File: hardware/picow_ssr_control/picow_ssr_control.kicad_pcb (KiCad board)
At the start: 2 copper layers, 65 x 90 mm, 33 parts, among them Q1 DMG2301L, Q2 DMG2301L, U1 RaspberryPi-PicoW, U2 ULN2803A

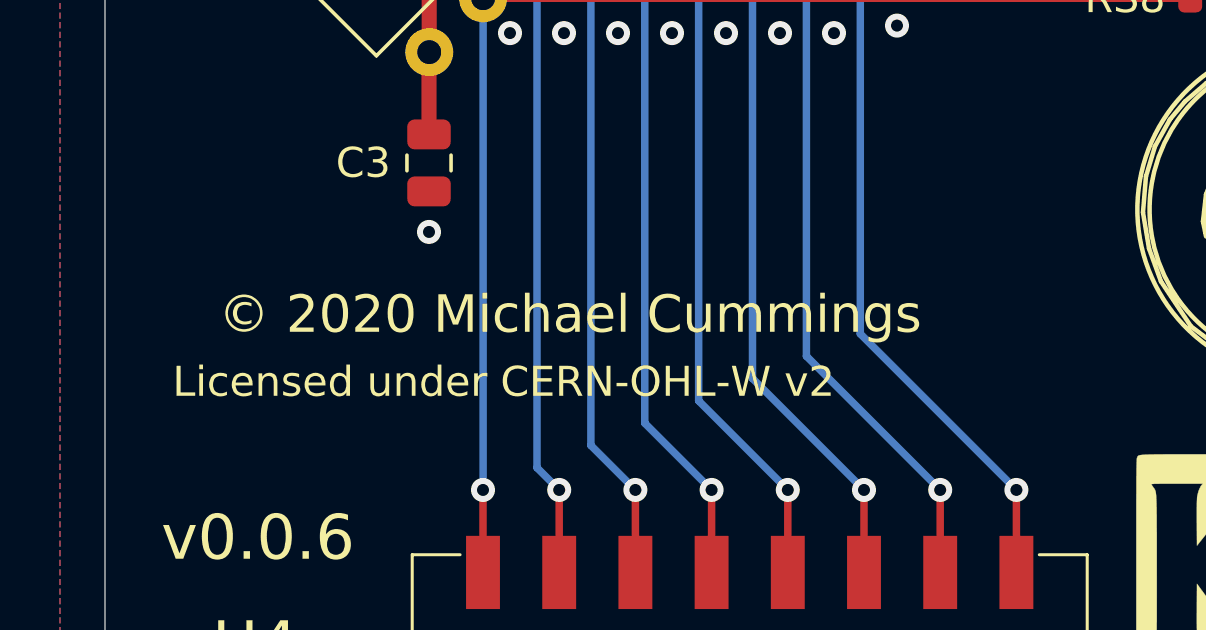
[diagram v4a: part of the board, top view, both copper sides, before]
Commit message: Fixed incorrect copyright date on PCB
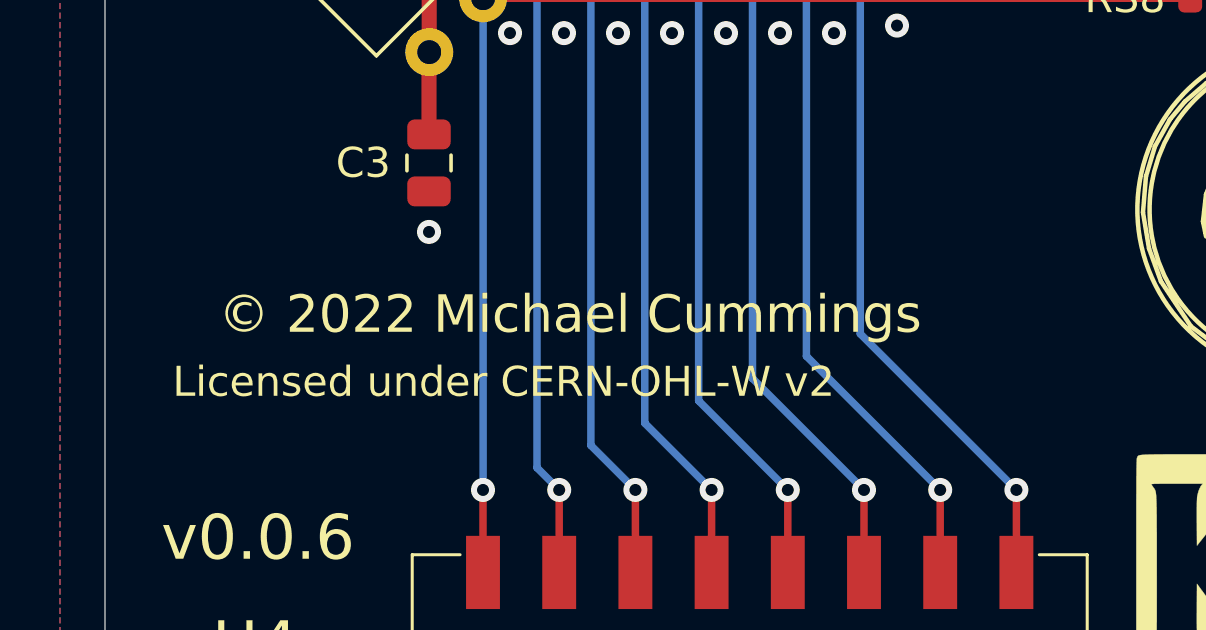
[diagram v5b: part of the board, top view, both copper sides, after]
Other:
- board text added: "© 2022 Michael Cummings"
- board text removed: "© 2020 Michael Cummings"
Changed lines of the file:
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@@
   (gr_rect (start 50 50) (end 115 140) (layer "User.9") (width 0.15) (fill none))
   (gr_circle (center 110 135) (end 111.55 135) (layer "User.9") (width 0.15) (fill none))
-  (gr_text "© 2020 Michael Cummings" (at 65.5 119.5) (layer "F.SilkS")
+  (gr_text "© 2022 Michael Cummings" (at 65.5 119.5) (layer "F.SilkS")
     (effects (font (size 1.25 1.25) (thickness 0.25)))
   )

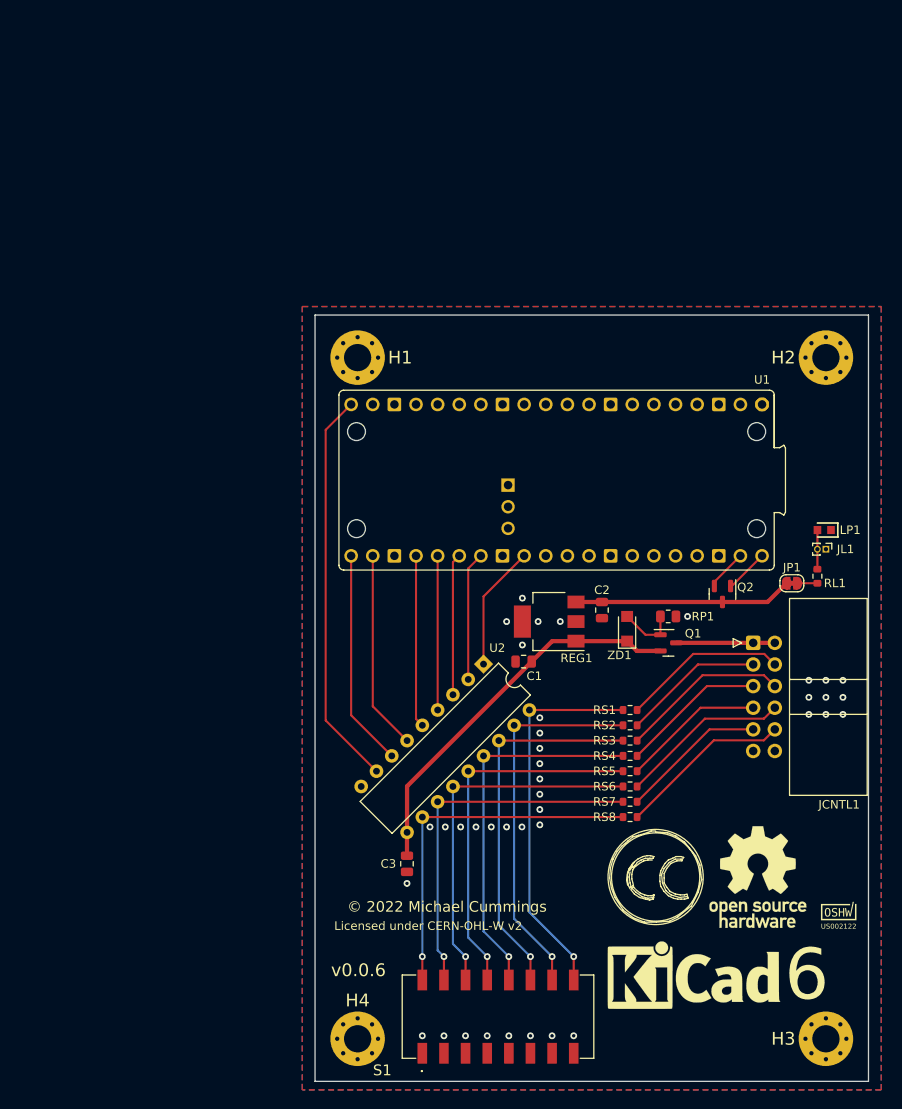
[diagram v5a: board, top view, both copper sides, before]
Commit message: WIP control connector changes v0.0.7
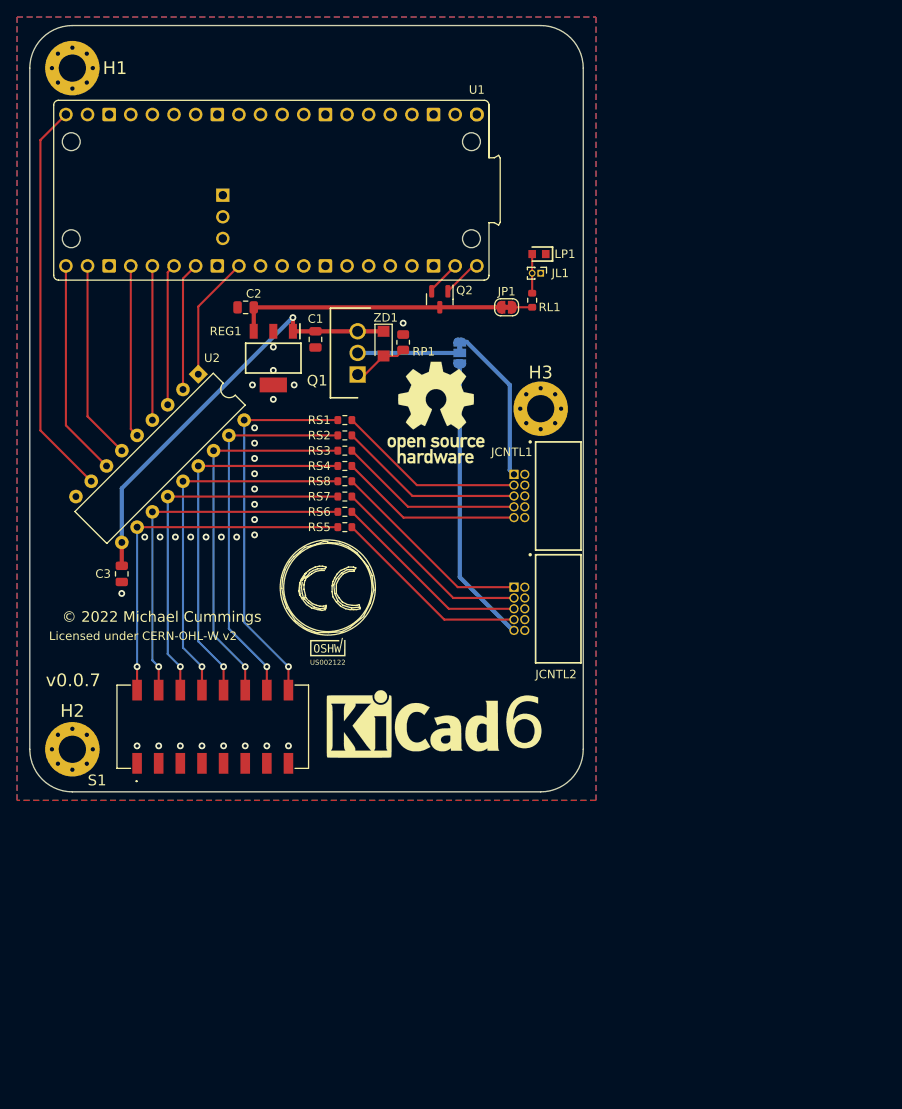
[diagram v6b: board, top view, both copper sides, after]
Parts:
- removed H4: MountingHole_Pad, MountingHole:MountingHole_3.2mm_M3_Pad_Via
- added JCNTL2: SHF-105-01-L-D-RA, dragon_mobile:SAMTEC_SHF-105-01-L-D-RA, F.Cu at (74.0, 84.5)
- added JS1: SolderJumper_3_Bridged12, Jumper:SolderJumper-3_P1.3mm_Bridged12_RoundedPad1.0x1.5mm_NumberLabels, B.Cu at (67.0, 54.5)
- JCNTL1: value Conn_02x06_Odd_Even -> SHF-105-01-L-D-RA; footprint Connector_IDC:IDC-Header_2x06_P2.54mm_Horizontal -> dragon_mobile:SAMTEC_SHF-105-01-L-D-RA
- Q1: value DMG2301L -> IRF4905PBF; footprint Package_TO_SOT_SMD:SOT-23 -> dragon_mobile:TO254P469X1042X1967-3P
- Q2: footprint Package_TO_SOT_SMD:SOT-23 -> Picow_control:DMG2301L
- REG1: footprint Package_TO_SOT_SMD:SOT-223 -> SamacSys_Parts:SOT230P700X180-4N
- RS1, RS2, RS3, RS4: value 25 -> 270
- RS5: renamed from RS8; value 25 -> 270
- RS6: renamed from RS7; value 25 -> 270
- RS7: renamed from RS6; value 25 -> 270
- RS8: renamed from RS5; value 25 -> 270
- moved H2 99.7 mm to (21.5, 101.0)
- moved H3 81.2 mm to (76.5, 61.0)
- moved OSHW_Mono_0.1_Scale 67.5 mm to (51.5, 89.0)
- moved #LOGO1 66.4 mm to (64.2, 61.5)
- moved C2 54.9 mm to (41.9, 49.1), turned to 180 degrees
- moved #LOGO2 51.4 mm to (51.5, 82.0)
- moved Q1 48.2 mm to (55.0, 57.0), turned to 90 degrees
- moved Q2 48.0 mm to (64.7, 48.1)
- moved RS1 47.8 mm to (53.5, 62.3), turned to 0 degrees
- moved S1 47.8 mm to (38.0, 98.3)
- moved U2 47.8 mm to (36.3, 57.0)
- moved C3 47.8 mm to (27.3, 80.4)
- moved QRCode1 47.8 mm to (55.2, 77.0)
- moved RS2 47.8 mm to (53.5, 64.1)
- moved RS3 47.8 mm to (53.5, 65.9), turned to 0 degrees
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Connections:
- JCNTL1 pad 1: +BATT -> Net-(JCNTL1-Pad1)
- JCNTL1 pad 10: Net-(JCNTL1-Pad10) -> GNDPWR
- JCNTL1 pad 2: +BATT -> GNDPWR
- JCNTL1 pad 4: Net-(JCNTL1-Pad4) -> GNDPWR
- JCNTL1 pad 6: Net-(JCNTL1-Pad6) -> GNDPWR
- JCNTL1 pad 8: Net-(JCNTL1-Pad8) -> GNDPWR
- Q1 pad 2: +VDC -> +BATT
- Q1 pad 3: +BATT -> +VDC
- RS1 pad 1: Net-(JCNTL1-Pad4) -> /a1
- RS1 pad 2: /a1 -> Net-(JCNTL1-Pad3)
- RS2 pad 2: Net-(JCNTL1-Pad3) -> Net-(JCNTL1-Pad5)
- RS3 pad 1: Net-(JCNTL1-Pad6) -> /a3
- RS3 pad 2: /a3 -> Net-(JCNTL1-Pad7)
- RS4 pad 1: /a4 -> Net-(JCNTL1-Pad9)
- RS4 pad 2: Net-(JCNTL1-Pad5) -> /a4
- RS5 pad 1: Net-(JCNTL1-Pad10) -> /a5
- RS5 pad 2: /a8 -> Net-(JCNTL2-Pad7)
- RS6 pad 1: /a7 -> /a6
- RS6 pad 2: Net-(JCNTL1-Pad9) -> Net-(JCNTL2-Pad5)
- RS7 pad 1: Net-(JCNTL1-Pad8) -> /a7
- RS7 pad 2: /a6 -> Net-(JCNTL2-Pad3)
- RS8 pad 1: /a5 -> /a8
- RS8 pad 2: Net-(JCNTL1-Pad7) -> Net-(JCNTL2-Pad1)
- S1 pad 13: /a5 -> /a8
- S1 pad 14: /a6 -> /a7
- S1 pad 15: /a7 -> /a6
- S1 pad 16: /a8 -> /a5
- U2 pad 11: /a8 -> /a5
- U2 pad 12: /a7 -> /a6
- U2 pad 13: /a6 -> /a7
- U2 pad 14: /a5 -> /a8
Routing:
- net Net-(JCNTL2-Pad9): track 0.00 -> 33.9 mm
- net Net-(JCNTL2-Pad1): track 0.00 -> 24.2 mm
- net Net-(JCNTL2-Pad3): track 0.00 -> 24.0 mm
- net Net-(JCNTL2-Pad5): track 0.00 -> 23.8 mm
- net Net-(JCNTL2-Pad7): track 0.00 -> 23.5 mm
- net Net-(JCNTL1-Pad10): track 20.4 -> 0.00 mm
- net Net-(JCNTL1-Pad8): track 20.0 -> 0.00 mm
- net Net-(JCNTL1-Pad6): track 19.9 -> 0.00 mm
- net Net-(JCNTL1-Pad4): track 19.4 -> 0.00 mm
- net Net-(JCNTL1-Pad1): track 0.00 -> 18.7 mm
- net +5V: track 25.6 -> 31.8 mm
- net Net-(JCNTL1-Pad3): track 16.6 -> 22.2 mm
- net Net-(JCNTL1-Pad7): track 16.7 -> 21.8 mm
- net Net-(JCNTL1-Pad5): track 17.0 -> 22.0 mm
- net Net-(JCNTL1-Pad9): track 17.2 -> 21.6 mm
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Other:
- outline, holes or cut-outs redrawn
- board text added: "0"
- board text added: "0 mm"
- board text added: "0.01 mm"
- board text added: "0.02"
- board text added: "0.07 mm"
- board text added: "0.2000 mm / 0.2000 mm"
- board text added: "1"
- board text added: "1.2 mm"
- board text added: "1.3600 mm"
- board text added: "3.3"
- board text added: "4.5"
- board text added: "B.Cu"
- board text added: "B.Mask"
- board text added: "B.Paste"
- board text added: "B.Silkscreen"
- board text added: "Bottom Silk Screen"
- board text added: "Bottom Solder Mask"
- board text added: "Bottom Solder Paste"
- board text added: "Color"
- board text added: "Dielectric 1"
- board text added: "Epsilon R"
- board text added: "F.Cu"
- board text added: "F.Mask"
- board text added: "F.Paste"
- board text added: "F.Silkscreen"
- board text added: "FR4"
- board text added: "Green"
- board text added: "Layer Name"
- board text added: "Liquid Ink"
- board text added: "Liquid Photo"
- board text added: "Loss Tangent"
- board text added: "Material"
- board text added: "Thickness (mm)"
- board text added: "Top Silk Screen"
- board text added: "Top Solder Mask"
- board text added: "Top Solder Paste"
- board text added: "Type"
- board text added: "White"
- board text added: "copper"
- board text added: "core"
- board text added: "v0.0.7"
- board text removed: "0.2000 mm / 0.0000 mm"
- board text removed: "1.7600 mm"
- board text removed: "v0.0.6"

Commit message: Replaced un-obtainable ULN2803 with SMD FETs and updated control connectors
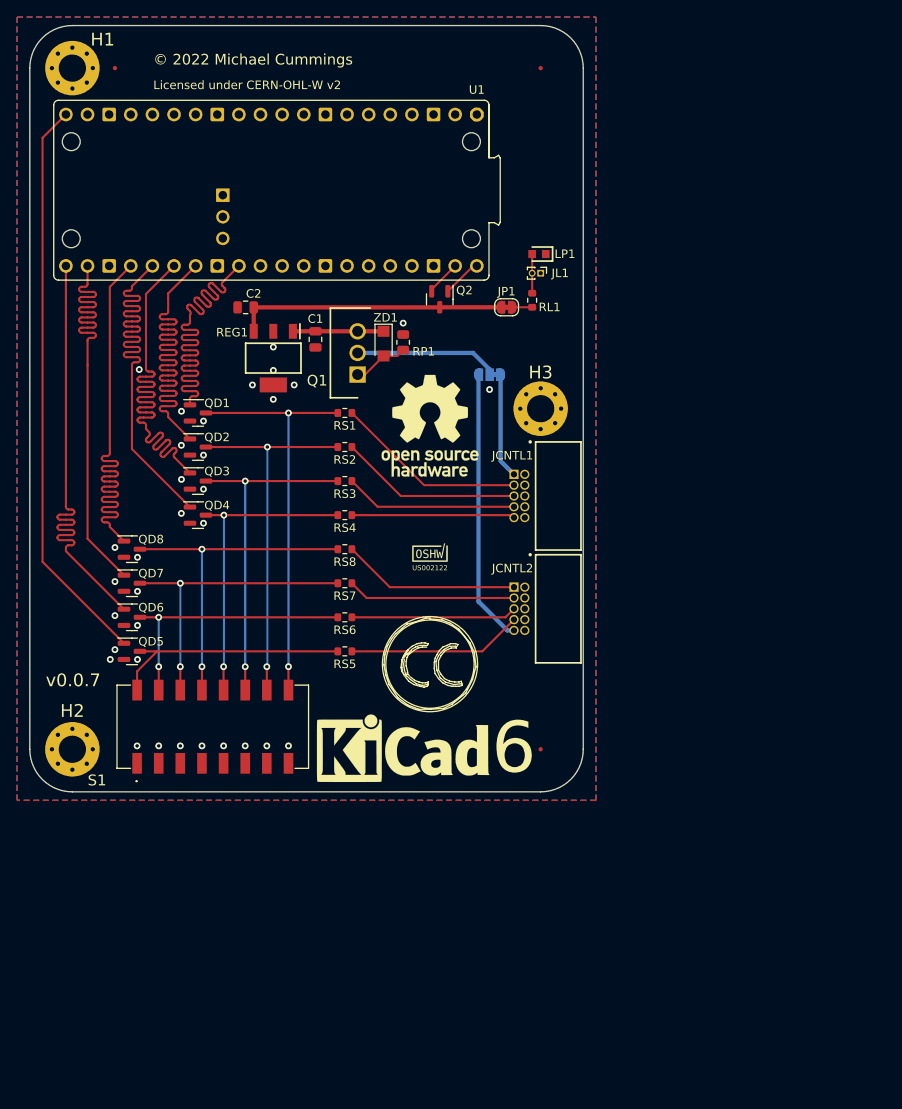
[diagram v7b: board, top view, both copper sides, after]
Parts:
- removed C3: 100n, Capacitor_SMD:C_0805_2012Metric
- removed U2: ULN2803A, Package_DIP:DIP-18_W7.62mm
- added FID1: Fiducial, Fiducial:Fiducial_0.5mm_Mask1mm, F.Cu at (26.5, 21.0)
- added FID2: Fiducial, Fiducial:Fiducial_0.5mm_Mask1mm, F.Cu at (76.5, 21.0)
- added FID3: Fiducial, Fiducial:Fiducial_0.5mm_Mask1mm, F.Cu at (76.5, 101.0)
- added QD1: 2N7002K, Package_TO_SOT_SMD:SOT-23, F.Cu at (36.2, 61.5)
- added QD2: 2N7002K, Package_TO_SOT_SMD:SOT-23, F.Cu at (36.2, 65.5)
- added QD3: 2N7002K, Package_TO_SOT_SMD:SOT-23, F.Cu at (36.2, 69.5)
- added QD4: 2N7002K, Package_TO_SOT_SMD:SOT-23, F.Cu at (36.2, 73.5)
- added QD5: 2N7002K, Package_TO_SOT_SMD:SOT-23, F.Cu at (28.5, 89.5)
- added QD6: 2N7002K, Package_TO_SOT_SMD:SOT-23, F.Cu at (28.5, 85.5)
- added QD7: 2N7002K, Package_TO_SOT_SMD:SOT-23, F.Cu at (28.5, 81.5)
- added QD8: 2N7002K, Package_TO_SOT_SMD:SOT-23, F.Cu at (28.5, 77.5)
- QRCode1: value LOGO -> GitHub URL
- moved OSHW_Mono_0.1_Scale 16.3 mm to (63.5, 77.9)
- moved #LOGO2 15.0 mm to (63.5, 91.0)
- moved RS5 14.6 mm to (53.5, 89.5)
- moved RS6 12.4 mm to (53.5, 85.5)
- moved RS7 10.2 mm to (53.5, 81.5)
- moved RS8 7.98 mm to (53.5, 77.5)
- moved RS4 5.77 mm to (53.5, 73.5)
- moved JS1 4.33 mm to (70.5, 57.0), turned to 180 degrees
- moved RS3 3.57 mm to (53.5, 69.5)
- moved #LOGO2 3.07 mm to (60.4, 100.8)
- moved QRCode1 1.83 mm to (57.0, 77.5)
- moved #LOGO1 1.70 mm to (63.5, 63.0)
- moved RS2 1.37 mm to (53.5, 65.5)
- moved RS1 0.84 mm to (53.5, 61.5)
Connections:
- U1 pad 20: Net-(U1-Pad20) -> /b5
- U1 pad 21: Net-(U1-Pad21) -> /b6
- U1 pad 22: Net-(U1-Pad22) -> /b7
- U1 pad 24: Net-(U1-Pad24) -> /b8
- U1 pad 25: Net-(U1-Pad25) -> /b4
- U1 pad 26: Net-(U1-Pad26) -> /b3
- U1 pad 27: Net-(U1-Pad27) -> /b2
- U1 pad 29: Net-(U1-Pad29) -> /b1
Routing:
- net /b5: track 0.00 -> 67.2 mm
- net /b6: track 0.00 -> 54.8 mm
- net /b7: track 0.00 -> 54.7 mm
- net /b8: track 0.00 -> 54.7 mm
- net /b4: track 0.00 -> 54.6 mm
- net /b2: track 0.00 -> 54.5 mm
- net /b3: track 0.00 -> 54.5 mm
- net /b1: track 0.00 -> 54.4 mm
- net Net-(U1-Pad20): track 46.8 -> 0.00 mm
- net +VDC: track 49.7 -> 10.6 mm, vias 1 -> 0
- net Net-(U1-Pad21): track 25.5 -> 0.00 mm
- net Net-(U1-Pad22): track 23.4 -> 0.00 mm
- net Net-(U1-Pad24): track 20.2 -> 0.00 mm
- net Net-(U1-Pad25): track 18.1 -> 0.00 mm
- net Net-(U1-Pad26): track 16.6 -> 0.00 mm
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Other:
- board text added: "0.2000 mm / 0.1800 mm"
- board text added: "1.1600 mm"
- board text removed: "0"
- board text removed: "0 mm"
- board text removed: "0.01 mm"
- board text removed: "0.02"
- board text removed: "0.07 mm"
- board text removed: "0.2000 mm / 0.2000 mm"
- board text removed: "1"
- board text removed: "1.2 mm"
- board text removed: "1.3600 mm"
- board text removed: "3.3"
- board text removed: "4.5"
- board text removed: "B.Cu"
- board text removed: "B.Mask"
- board text removed: "B.Paste"
- board text removed: "B.Silkscreen"
- board text removed: "Bottom Silk Screen"
- board text removed: "Bottom Solder Mask"
- board text removed: "Bottom Solder Paste"
- board text removed: "Color"
- board text removed: "Dielectric 1"
- board text removed: "Epsilon R"
- board text removed: "F.Cu"
- board text removed: "F.Mask"
- board text removed: "F.Paste"
- board text removed: "F.Silkscreen"
- board text removed: "FR4"
- board text removed: "Green"
- board text removed: "Layer Name"
- board text removed: "Liquid Ink"
- board text removed: "Liquid Photo"
- board text removed: "Loss Tangent"
- board text removed: "Material"
- board text removed: "Thickness (mm)"
- board text removed: "Top Silk Screen"
- board text removed: "Top Solder Mask"
- board text removed: "Top Solder Paste"
- board text removed: "Type"
- board text removed: "White"
- board text removed: "copper"
- board text removed: "core"

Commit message: Misc minor updates after tag
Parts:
- added JS2: Conn_01x02, Connector_PinHeader_1.00mm:PinHeader_1x02_P1.00mm_Vertical, F.Cu at (65.4, 54.5)
- moved Q2 2.76 mm to (67.4, 48.1)
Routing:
- net Net-(U1-Pad40): track 4.22 -> 3.25 mm
- net Net-(U1-Pad39): track 3.90 -> 2.98 mm
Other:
- board text added: "Mounting holes are for M3 screws and should be drill at 2.5mm (#39) and tapped at .5mm threads. Additional support for the two corners without mounting holes may be needed in high vibration enviroments."
- board text removed: "Mounting holes are for M3 screws and should be drill at 2.5mm (#39) and tapped at .5mm threads."
